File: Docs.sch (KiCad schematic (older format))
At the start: 0 parts

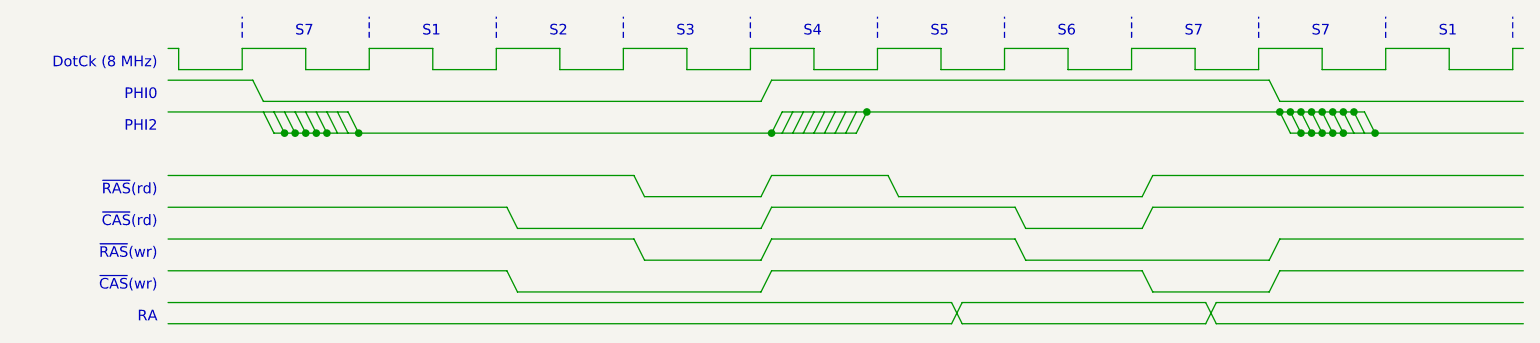
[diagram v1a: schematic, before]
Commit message: Updated timing diagram in docs
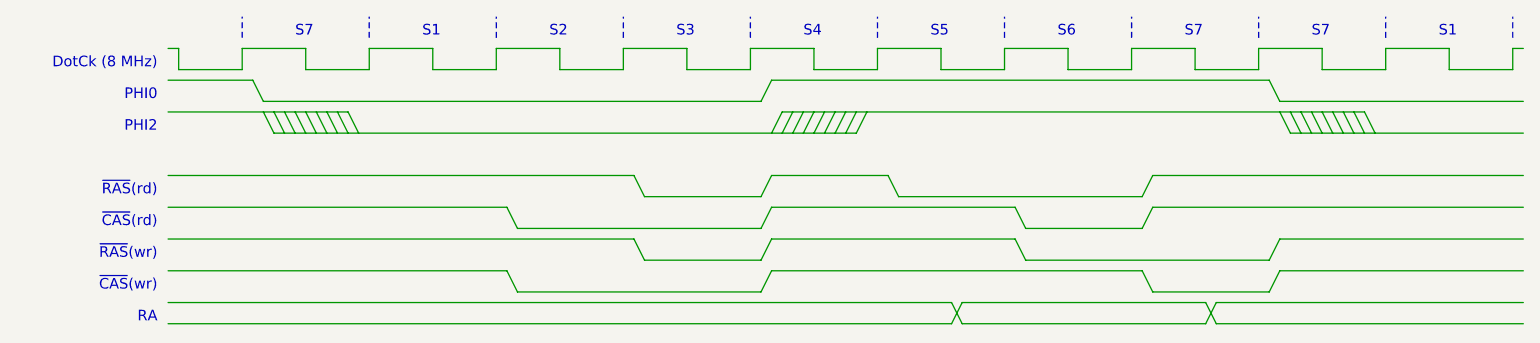
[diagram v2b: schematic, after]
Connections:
- wire segments 151 -> 129
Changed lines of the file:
@@
 Wire Wire Line
 	6350 1450 7500 1450
-Wire Wire Line
-	4000 1500 4400 1500
 Text Notes 1050 1300 2    50   ~ 0
 DotCk (8 MHz)
@@
 	1550 1450 3900 1450
 Wire Wire Line
-	1600 1500 1650 1600
-Wire Wire Line
 	1650 1500 1700 1600
 Wire Wire Line
-	1700 1500 1750 1600
-Wire Wire Line
 	1750 1500 1800 1600
 Wire Wire Line
 	1800 1500 1850 1600
 Wire Wire Line
-	1600 1600 1650 1600
-Wire Wire Line
 	3950 1600 4000 1500
-Connection ~ 1650 1600
-Wire Wire Line
-	1650 1600 1700 1600
-Connection ~ 1700 1600
-Wire Wire Line
-	1700 1600 1750 1600
-Connection ~ 1750 1600
-Wire Wire Line
-	1750 1600 1800 1600
-Connection ~ 1800 1600
-Wire Wire Line
-	1800 1600 1850 1600
-Connection ~ 1850 1600
-Wire Wire Line
-	3950 1600 4350 1600
 Wire Wire Line
 	4350 1600 4400 1500
-Connection ~ 3950 1600
-Connection ~ 4400 1500
 Wire Wire Line
 	4000 1600 4050 1500
@@
 	4300 1600 4350 1500
 Wire Wire Line
-	1850 1500 1900 1600
-Wire Wire Line
 	1900 1500 1950 1600
-Wire Wire Line
-	2000 1600 3950 1600
-Wire Wire Line
-	1850 1600 2000 1600
-Connection ~ 2000 1600
 Wire Wire Line
 	1950 1500 2000 1600
@@
 	6500 1500 6550 1600
 Wire Wire Line
-	6550 1500 6600 1600
-Wire Wire Line
 	6600 1500 6650 1600
 Wire Wire Line
-	6400 1600 6450 1600
-Connection ~ 6450 1600
-Wire Wire Line
-	6450 1600 6500 1600
-Connection ~ 6500 1600
-Wire Wire Line
-	6500 1600 6550 1600
-Connection ~ 6550 1600
-Wire Wire Line
-	6550 1600 6600 1600
-Connection ~ 6600 1600
-Wire Wire Line
-	6600 1600 6650 1600
-Connection ~ 6650 1600
-Wire Wire Line
 	6650 1500 6700 1600
 Wire Wire Line
 	6700 1500 6750 1600
 Wire Wire Line
-	6800 1600 7500 1600
-Wire Wire Line
-	6650 1600 6800 1600
-Connection ~ 6800 1600
-Wire Wire Line
 	6750 1500 6800 1600
-Wire Wire Line
-	4400 1500 6350 1500
-Connection ~ 6350 1500
-Wire Wire Line
-	6350 1500 6400 1500
-Connection ~ 6400 1500
-Wire Wire Line
-	6400 1500 6450 1500
-Connection ~ 6450 1500
-Wire Wire Line
-	6450 1500 6500 1500
-Connection ~ 6500 1500
-Wire Wire Line
-	6500 1500 6550 1500
-Connection ~ 6550 1500
-Wire Wire Line
-	6550 1500 6600 1500
-Connection ~ 6600 1500
-Wire Wire Line
-	6600 1500 6650 1500
-Connection ~ 6650 1500
-Wire Wire Line
-	6650 1500 6700 1500
-Connection ~ 6700 1500
-Wire Wire Line
-	6700 1500 6750 1500
 Wire Wire Line
 	5150 2050 5700 2050
@@
 Wire Wire Line
 	3950 2100 5100 2100
+Wire Wire Line
+	1700 1500 1750 1600
+Wire Wire Line
+	1600 1500 1650 1600
+Wire Wire Line
+	1850 1500 1900 1600
+Wire Wire Line
+	1600 1600 4350 1600
+Wire Wire Line
+	4000 1500 6750 1500
+Wire Wire Line
+	6550 1500 6600 1600
+Wire Wire Line
+	6400 1600 7500 1600
 $EndSCHEMATC
